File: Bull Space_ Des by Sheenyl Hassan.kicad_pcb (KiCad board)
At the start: 2 copper layers, 10 parts, among them IC1 TEENSY_4.0, IC2 XB24CZ7PIT-004, U1 Regulator_Linear_AP2204RB-3.3, U2 Flight-Computer_Adafruit_GPS_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, U3 ADXL343, U4 BMP280, U6 Memory_Flash_W25Q32JVSS

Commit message: Add files via upload
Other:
- net class Default removed

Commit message: Updates
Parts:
- moved IC1 53.4 mm to (81.3, 114.3)
- moved IC2 50.0 mm to (206.8, 109.7)
- moved U2 36.5 mm to (99.9, 142.2)
- moved U3 32.6 mm to (165.1, 114.3)
- moved U1 30.5 mm to (182.9, 81.3)
- moved U6 21.3 mm to (147.3, 142.2)
- moved U4 20.3 mm to (119.4, 86.4)
- moved C1 12.0 mm to (142.2, 99.1)
- moved C5 10.9 mm to (154.9, 78.7)
- moved R1 9.67 mm to (157.5, 129.5)
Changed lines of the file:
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@@
   (net 68 "Net-(U2-Pad9)")
   (footprint "KiCad:TEENSY40" (layer "F.Cu")
-    (at 134.62 115.57)
+    (at 81.28 114.3)
     (descr "TEENSY 4.0-4")
     (tags "Integrated Circuit")
@@
   )
   (footprint "Package_LGA:LGA-14_3x5mm_P0.8mm_LayoutBorder1x6y" (layer "F.Cu")
-    (at 153.67 83.82 90)
+    (at 165.1 114.3 90)
     (descr "LGA, 14 Pin (http://www.st.com/resource/en/datasheet/lsm303dlhc.pdf), generated with kicad-footprint-generator ipc_noLead_generator.py")
     (tags "LGA NoLead")
@@
   )
   (footprint "Package_SO:SOIC-8_5.23x5.23mm_P1.27mm" (layer "F.Cu")
-    (at 153.67 121.92)
+    (at 147.32 142.24)
     (descr "SOIC, 8 Pin (http://www.winbond.com/resource-files/w25q32jv%20revg%2003272018%20plus.pdf#page=68), generated with kicad-footprint-generator ipc_gullwing_generator.py")
     (tags "SOIC SO")
@@
   )
   (footprint "Capacitor_SMD:C_0603_1608Metric_Pad1.08x0.95mm_HandSolder" (layer "F.Cu")
-    (at 146.05 87.63 180)
+    (at 142.24 99.06 180)
     (descr "Capacitor SMD 0603 (1608 Metric), square (rectangular) end terminal, IPC_7351 nominal with elongated pad for handsoldering. (Body size source: IPC-SM-782 page 76, https://www.pcb-3d.com/wordpress/wp-content/uploads/ipc-sm-782a_amendment_1_and_2.pdf), generated with kicad-footprint-generator")
     (tags "capacitor handsolder")
@@
   )
   (footprint "Capacitor_SMD:C_0603_1608Metric_Pad1.08x0.95mm_HandSolder" (layer "F.Cu")
-    (at 146.05 85.12 180)
+    (at 154.94 78.74 180)
     (descr "Capacitor SMD 0603 (1608 Metric), square (rectangular) end terminal, IPC_7351 nominal with elongated pad for handsoldering. (Body size source: IPC-SM-782 page 76, https://www.pcb-3d.com/wordpress/wp-content/uploads/ipc-sm-782a_amendment_1_and_2.pdf), generated with kicad-footprint-generator")
     (tags "capacitor handsolder")
@@
   )
   (footprint "Package_TO_SOT_SMD:SOT-89-3" (layer "F.Cu")
-    (at 153.67 90.17 -90)
+    (at 182.88 81.28 -90)
     (descr "SOT-89-3, http://ww1.microchip.com/downloads/en/DeviceDoc/3L_SOT-89_MB_C04-029C.pdf")
     (tags "SOT-89-3")
@@
   )
   (footprint "Resistor_SMD:R_0603_1608Metric_Pad0.98x0.95mm_HandSolder" (layer "F.Cu")
-    (at 161.29 120.65 -90)
+    (at 157.48 129.54 -90)
     (descr "Resistor SMD 0603 (1608 Metric), square (rectangular) end terminal, IPC_7351 nominal with elongated pad for handsoldering. (Body size source: IPC-SM-782 page 72, https://www.pcb-3d.com/wordpress/wp-content/uploads/ipc-sm-782a_amendment_1_and_2.pdf), generated with kicad-footprint-generator")
     (tags "resistor handsolder")
@@
   )
   (footprint "KiCad:XB24CAPIT-001" (layer "F.Cu")
-    (at 162.56 86.36 -90)
+    (at 206.77 109.702955 -90)
     (descr "Digi XBee 802.15.4")
     (tags "Integrated Circuit")
@@
   )
   (footprint "KiCad:Flight-Computer_Adafruit_GPS_THT_Footprint" (layer "F.Cu")
-    (at 134.62 130.81 -90)
+    (at 99.917 142.24 -90)
     (attr through_hole)
     (fp_text reference "U2" (at 0.508 2.032 90) (layer "F.SilkS")
@@
   )
   (footprint "Package_LGA:Bosch_LGA-8_2x2.5mm_P0.65mm_ClockwisePinNumbering" (layer "F.Cu")
-    (at 139.7 86.36)
+    (at 119.38 86.36)
     (descr "LGA-8, https://ae-bst.resource.bosch.com/media/_tech/media/datasheets/BST-BMP280-DS001-18.pdf")
     (tags "lga land grid array")

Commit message: Added Ignition
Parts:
- added BZ1: Buzzer, Buzzer_Beeper:Buzzer_12x9.5RM7.6, F.Cu at (103.1, 74.4)
- added C2: 1uf, Capacitor_SMD:C_0805_2012Metric_Pad1.18x1.45mm_HandSolder, F.Cu at (78.7, 127.0)
- added C3: 22uf, Capacitor_SMD:C_0805_2012Metric_Pad1.18x1.45mm_HandSolder, F.Cu at (47.2, 96.8)
- added C4: 47pf, Capacitor_SMD:C_0805_2012Metric_Pad1.18x1.45mm_HandSolder, F.Cu at (84.1, 131.6)
- added D1: LED_ABGR, LED_THT:LED_D5.0mm-4_RGB_Staggered_Pins, F.Cu at (112.6, 43.2)
- added J1: Screw_Terminal_01x02, TerminalBlock:TerminalBlock_bornier-2_P5.08mm, F.Cu at (80.8, 40.6)
- added J2: Screw_Terminal_01x02, TerminalBlock:TerminalBlock_bornier-2_P5.08mm, F.Cu at (80.8, 52.7)
- added R2: 220, Resistor_SMD:R_0603_1608Metric_Pad0.98x0.95mm_HandSolder, F.Cu at (124.0, 50.5)
- added R3: 220, Resistor_SMD:R_0603_1608Metric_Pad0.98x0.95mm_HandSolder, F.Cu at (127.0, 45.7)
- added R4: 220, Resistor_SMD:R_0603_1608Metric_Pad0.98x0.95mm_HandSolder, F.Cu at (122.9, 40.6)
- C1, C5: footprint Capacitor_SMD:C_0603_1608Metric_Pad1.08x0.95mm_HandSolder -> Capacitor_SMD:C_0805_2012Metric_Pad1.18x1.45mm_HandSolder
- IC1: footprint KiCad:TEENSY40 -> Flight Computer:Teensy40
- IC2: footprint KiCad:XB24CAPIT-001 -> Flight Computer:XBEE_PRO_PTH
- U2: footprint KiCad:Flight-Computer_Adafruit_GPS_THT_Footprint -> Flight Computer:Adafruit_ADXL345_THT
- moved IC2 125.9 mm to (81.3, 119.4), turned to 0 degrees
- moved U3 114.3 mm to (50.8, 111.8), turned to 180 degrees
- moved U6 100.1 mm to (55.9, 101.6)
- moved R1 95.6 mm to (66.0, 101.6), turned to 180 degrees
- moved U4 75.4 mm to (55.9, 127.0)
- moved U1 53.8 mm to (130.6, 68.6)
- moved C1 39.3 mm to (125.5, 63.5)
- moved U2 38.3 mm to (96.0, 104.1)
- moved IC1 25.4 mm to (81.3, 88.9), turned to -90 degrees
- moved C5 24.0 mm to (136.4, 63.5)
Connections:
- net XBEE-RX renamed /XBEE-TX
- net XBEE-TX renamed /XBEE-RX
- IC1 pad 10: Net-(IC1-Pad10) -> /FL-CS
- IC1 pad 11: Net-(IC1-Pad11) -> /BMP-CS
- IC1 pad 12: FL-CS -> /ADXL-CS
- IC1 pad 13: MOSI -> /MOSI
- IC1 pad 14: MISO -> /MISO
- IC1 pad 15: Net-(IC1-Pad15) -> unconnected-(IC1-Pad15)
- IC1 pad 16: Net-(IC1-Pad16) -> +3V3
- IC1 pad 18: Net-(IC1-Pad18) -> unconnected-(IC1-Pad18)
- IC1 pad 19: Net-(IC1-Pad19) -> unconnected-(IC1-Pad19)
- IC1 pad 2: Net-(IC1-Pad2) -> unconnected-(IC1-Pad2)
- IC1 pad 20: SCK -> /SCK
- IC1 pad 23: SCL -> unconnected-(IC1-Pad23)
- IC1 pad 24: SDA -> unconnected-(IC1-Pad24)
- IC1 pad 25: Net-(IC1-Pad25) -> unconnected-(IC1-Pad25)
- IC1 pad 26: Net-(IC1-Pad26) -> unconnected-(IC1-Pad26)
- IC1 pad 27: Net-(IC1-Pad27) -> /GPS-RX
- IC1 pad 28: Net-(IC1-Pad28) -> /GPS-TX
- IC1 pad 29: Net-(IC1-Pad29) -> unconnected-(IC1-Pad29)
- IC1 pad 3: Net-(IC1-Pad3) -> unconnected-(IC1-Pad3)
- IC1 pad 30: Net-(IC1-Pad30) -> unconnected-(IC1-Pad30)
- IC1 pad 33: +5V -> unconnected-(IC1-Pad33)
- IC1 pad 4: Net-(IC1-Pad4) -> LED-R
- IC1 pad 5: Net-(IC1-Pad5) -> LED-G
- IC1 pad 6: Net-(IC1-Pad6) -> LED-B
- IC1 pad 7: Net-(IC1-Pad7) -> unconnected-(IC1-Pad7)
- IC1 pad 8: Net-(IC1-Pad8) -> unconnected-(IC1-Pad8)
- IC1 pad 9: Net-(IC1-Pad9) -> unconnected-(IC1-Pad9)
- IC2 pad 11: Net-(IC2-Pad11) -> unconnected-(IC2-Pad11)
- IC2 pad 12: Net-(IC2-Pad12) -> unconnected-(IC2-Pad12)
- IC2 pad 13: Net-(IC2-Pad13) -> unconnected-(IC2-Pad13)
- IC2 pad 14: Net-(IC2-Pad14) -> unconnected-(IC2-Pad14)
- IC2 pad 15: Net-(IC2-Pad15) -> unconnected-(IC2-Pad15)
- IC2 pad 16: Net-(IC2-Pad16) -> unconnected-(IC2-Pad16)
- IC2 pad 17: Net-(IC2-Pad17) -> unconnected-(IC2-Pad17)
- IC2 pad 18: Net-(IC2-Pad18) -> unconnected-(IC2-Pad18)
- IC2 pad 19: Net-(IC2-Pad19) -> unconnected-(IC2-Pad19)
- IC2 pad 20: Net-(IC2-Pad20) -> unconnected-(IC2-Pad20)
- IC2 pad 4: Net-(IC2-Pad4) -> unconnected-(IC2-Pad4)
- IC2 pad 5: Net-(IC2-Pad5) -> unconnected-(IC2-Pad5)
- IC2 pad 6: Net-(IC2-Pad6) -> unconnected-(IC2-Pad6)
- IC2 pad 7: Net-(IC2-Pad7) -> unconnected-(IC2-Pad7)
- IC2 pad 8: Net-(IC2-Pad8) -> unconnected-(IC2-Pad8)
- IC2 pad 9: Net-(IC2-Pad9) -> unconnected-(IC2-Pad9)
- U2 pad 2: Net-(U2-Pad2) -> unconnected-(U2-Pad2)
- U2 pad 3: Net-(U2-Pad3) -> unconnected-(U2-Pad3)
- U2 pad 4: Net-(U2-Pad4) -> unconnected-(U2-Pad4)
- U2 pad 5: SDA -> /GPS-TX
- U2 pad 6: SCL -> /GPS-RX
- U2 pad 8: Net-(U2-Pad8) -> unconnected-(U2-Pad8)
- U2 pad 9: Net-(U2-Pad9) -> unconnected-(U2-Pad9)
- U3 pad 1: Net-(U3-Pad1) -> +3V3
- U3 pad 10: Net-(U3-Pad10) -> unconnected-(U3-Pad10)
- U3 pad 11: Net-(U3-Pad11) -> unconnected-(U3-Pad11)
- U3 pad 12: Net-(U3-Pad12) -> /MISO
- U3 pad 13: SDA -> /MOSI
- U3 pad 14: SCL -> /SCK
- U3 pad 3: Net-(U3-Pad3) -> unconnected-(U3-Pad3)
- U3 pad 7: Net-(U3-Pad7) -> /ADXL-CS
- U3 pad 8: Net-(U3-Pad8) -> unconnected-(U3-Pad8)
- U3 pad 9: Net-(U3-Pad9) -> unconnected-(U3-Pad9)
- U4 pad 2: Net-(U4-Pad2) -> /BMP-CS
- U4 pad 3: SDA -> /MOSI
- U4 pad 4: SCL -> /SCK
- U4 pad 5: Net-(U4-Pad5) -> /MISO
- U4 pad 6: Net-(U4-Pad6) -> +3V3
- U4 pad 7: Net-(U4-Pad7) -> GND
- U4 pad 8: Net-(U4-Pad8) -> +3V3
- U6 pad 1: FL-CS -> /FL-CS
- U6 pad 2: MISO -> /MISO
- U6 pad 3: Net-(U6-Pad3) -> unconnected-(U6-Pad3)
- U6 pad 5: MOSI -> /MOSI
- U6 pad 6: SCK -> /SCK
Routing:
- net +3V3: track 0.00 -> 15.5 mm
- net Net-(R1-Pad2): track 0.00 -> 5.91 mm

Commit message: Board Layout (kinda)
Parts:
- removed J2: Screw_Terminal_01x02, TerminalBlock:TerminalBlock_bornier-2_P5.08mm
- added F1: 3A Polyfuse, Fuse:Fuse_1206_3216Metric_Pad1.42x1.75mm_HandSolder, F.Cu at (87.5, 127.8)
- added F2: 3A Polyfuse, Fuse:Fuse_1206_3216Metric_Pad1.42x1.75mm_HandSolder, F.Cu at (81.8, 128.0)
- added H1: MountingHole, MountingHole:MountingHole_2.7mm_M2.5, F.Cu at (113.8, 138.0)
- added H2: MountingHole, MountingHole:MountingHole_2.7mm_M2.5, F.Cu at (114.0, 67.0)
- added H3: MountingHole, MountingHole:MountingHole_2.7mm_M2.5, F.Cu at (75.0, 138.0)
- added Q1: AOI21357, Package_TO_SOT_THT:TO-251-3_Vertical, F.Cu at (105.6, 121.0)
- added Q2: 2N7002, Package_TO_SOT_SMD:SOT-23, F.Cu at (89.3, 123.8)
- added Q3: 2N7002, Package_TO_SOT_SMD:SOT-23, F.Cu at (98.2, 123.5)
- added Q4: 2N7002, Package_TO_SOT_SMD:SOT-23, F.Cu at (83.5, 123.2)
- added Q5: AOI21357, Package_TO_SOT_THT:TO-251-3_Vertical, F.Cu at (105.6, 113.3)
- added R10: 10k, Resistor_SMD:R_0603_1608Metric_Pad0.98x0.95mm_HandSolder, F.Cu at (86.0, 134.5)
- added R12: 10k, Resistor_SMD:R_0603_1608Metric_Pad0.98x0.95mm_HandSolder, F.Cu at (84.0, 131.8)
- added R5: 100R, Resistor_SMD:R_0603_1608Metric_Pad0.98x0.95mm_HandSolder, F.Cu at (82.0, 136.0)
- added R6: 100R, Resistor_SMD:R_0603_1608Metric_Pad0.98x0.95mm_HandSolder, F.Cu at (80.5, 132.0)
- added R7: 100, Resistor_SMD:R_0603_1608Metric_Pad0.98x0.95mm_HandSolder, F.Cu at (94.2, 127.5)
- added R8: 10k, Resistor_SMD:R_0603_1608Metric_Pad0.98x0.95mm_HandSolder, F.Cu at (86.8, 139.2)
- added R9: 10k, Resistor_SMD:R_0603_1608Metric_Pad0.98x0.95mm_HandSolder, F.Cu at (87.5, 131.5)
- C1: value 1uf -> 10uf
- J1: value Screw_Terminal_01x02 -> Screw_Terminal_01x06; footprint TerminalBlock:TerminalBlock_bornier-2_P5.08mm -> TerminalBlock_4Ucon:TerminalBlock_4Ucon_1x06_P3.50mm_Horizontal
- U1: value Regulator_Linear_AP2204RB-3.3 -> VXO7803-1000; footprint Package_TO_SOT_SMD:SOT-89-3 -> Package_TO_SOT_THT:TO-220-3_Horizontal_TabDown
- U2: footprint Flight Computer:Adafruit_ADXL345_THT -> Flight Computer:Adafruit_GPS_THT
- moved J1 87.8 mm to (111.9, 122.8), turned to 90 degrees
- moved C5 64.2 mm to (101.2, 117.2), turned to 90 degrees
- moved BZ1 60.0 mm to (98.8, 134.2), turned to 180 degrees
- moved U4 58.4 mm to (81.5, 74.5)
- moved U1 58.0 mm to (98.7, 117.0), turned to 90 degrees
- moved C4 57.0 mm to (95.8, 75.8)
- moved C3 56.7 mm to (103.0, 86.2)
- moved C1 55.1 mm to (101.2, 113.0), turned to -90 degrees
- moved C2 51.9 mm to (95.8, 78.0)
- moved IC2 49.7 mm to (103.2, 74.8)
- moved U6 48.5 mm to (103.0, 90.2)
- moved R1 44.9 mm to (109.2, 89.5), turned to -90 degrees
- moved R4 43.0 mm to (94.0, 72.5), turned to -90 degrees
- moved R3 41.2 mm to (95.8, 72.5), turned to -90 degrees
- moved U3 39.6 mm to (81.5, 86.8)
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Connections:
- BZ1 pad 2: GND -> Net-(BZ1-Pad2)
- C1 pad 1: +3V3 -> +BATT
- C5 pad 1: 12V -> +3V3
- IC1 pad 7: unconnected-(IC1-Pad7) -> BUZZER
- IC1 pad 8: unconnected-(IC1-Pad8) -> /ACT1
- IC1 pad 9: unconnected-(IC1-Pad9) -> /ACT2
- J1 pad 1: BATT+ -> +BATT
- U1 pad 1: 12V -> +3V3
- U1 pad 3: +3V3 -> +BATT
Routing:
- net +3V3: track 15.5 -> 3.88 mm, vias 0 -> 1
- net /DROGUE_POW: track 0.00 -> 6.57 mm
- net /MAIN_POW: track 0.00 -> 6.30 mm
- net Net-(R1-Pad2): track 5.91 -> 0.00 mm
- added copper zone on B.Cu, net +3V3
- added copper zone on F.Cu, net GND
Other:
- board outline added: 45 x 77 mm

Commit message: Something
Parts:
- moved F2 30.3 mm to (111.8, 132.1), turned to 180 degrees
- moved F1 24.3 mm to (111.8, 127.0), turned to 180 degrees
- moved R7 15.8 mm to (78.7, 124.5), turned to 90 degrees
- moved R8 15.0 mm to (101.6, 137.2), turned to -90 degrees
- moved Q2 14.8 mm to (101.6, 132.1)
- moved R9 13.5 mm to (99.1, 124.5), turned to -90 degrees
- moved R12 12.4 mm to (94.0, 124.5), turned to -90 degrees
- moved R5 11.7 mm to (83.8, 124.5), turned to -90 degrees
- moved Q4 11.5 mm to (76.2, 132.1), turned to -90 degrees
- moved R6 11.3 mm to (88.9, 124.5), turned to -90 degrees
- moved BZ1 9.86 mm to (88.9, 134.6)
- moved Q3 9.54 mm to (94.0, 132.1)
- moved R10 8.41 mm to (94.0, 137.2), turned to -90 degrees
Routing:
- net GND: track 0.00 -> 45.4 mm, vias 0 -> 1
- net Net-(Q3-Pad3): track 0.00 -> 29.8 mm, vias 0 -> 2
- net Net-(Q2-Pad1): track 0.00 -> 21.9 mm
- net Net-(Q1-Pad1): track 0.00 -> 21.5 mm, vias 0 -> 2
- net Net-(F1-Pad2): track 0.00 -> 20.8 mm, vias 0 -> 1
- net Net-(F2-Pad2): track 0.00 -> 20.8 mm, vias 0 -> 1
- net Net-(Q3-Pad1): track 0.00 -> 19.0 mm
- net +BATT: track 0.00 -> 9.89 mm
- net Net-(Q4-Pad1): track 0.00 -> 6.43 mm
- net Net-(BZ1-Pad2): track 0.00 -> 5.76 mm
- net BUZZER: track 0.00 -> 1.63 mm, vias 0 -> 1
- net /ACT2: track 0.00 -> 1.63 mm, vias 0 -> 1
- net /ACT1: track 0.00 -> 1.63 mm, vias 0 -> 1

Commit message: Pyro Channels
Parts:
- moved F2 24.3 mm to (102.8, 109.5), turned to 90 degrees
- moved F1 13.5 mm to (102.8, 117.0), turned to -90 degrees
- moved C1 11.3 mm to (98.8, 102.0)
- moved U1 6.73 mm to (96.2, 110.8)
- moved C5 3.85 mm to (98.8, 114.3)
- moved Q1 1.44 mm to (106.2, 119.8)
- moved Q5 1.22 mm to (106.2, 112.2)
- moved U2 0.25 mm to (72.2, 115.2)
- moved J1 0.15 mm to (111.8, 122.8)
- moved R9 0.06 mm to (99.0, 124.5)
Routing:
- net GND: track 45.4 -> 0.00 mm, vias 1 -> 0
- net +BATT: track 9.89 -> 41.0 mm
- net Net-(Q3-Pad3): track 29.8 -> 2.58 mm, vias 2 -> 0
- net Net-(Q1-Pad1): track 21.5 -> 3.60 mm, vias 2 -> 1
- net Net-(F1-Pad2): track 20.8 -> 3.93 mm, vias 1 -> 0
- net Net-(F2-Pad2): track 20.8 -> 4.31 mm, vias 1 -> 0
- net +3V3: track 4.38 -> 7.12 mm, vias 1 -> 2
- net BUZZER: track 1.63 -> 0.00 mm, vias 1 -> 0
- net /ACT2: track 1.63 -> 0.00 mm, vias 1 -> 0
- net /ACT1: track 1.63 -> 0.00 mm, vias 1 -> 0
- net /DROGUE_POW: track 6.57 -> 5.74 mm

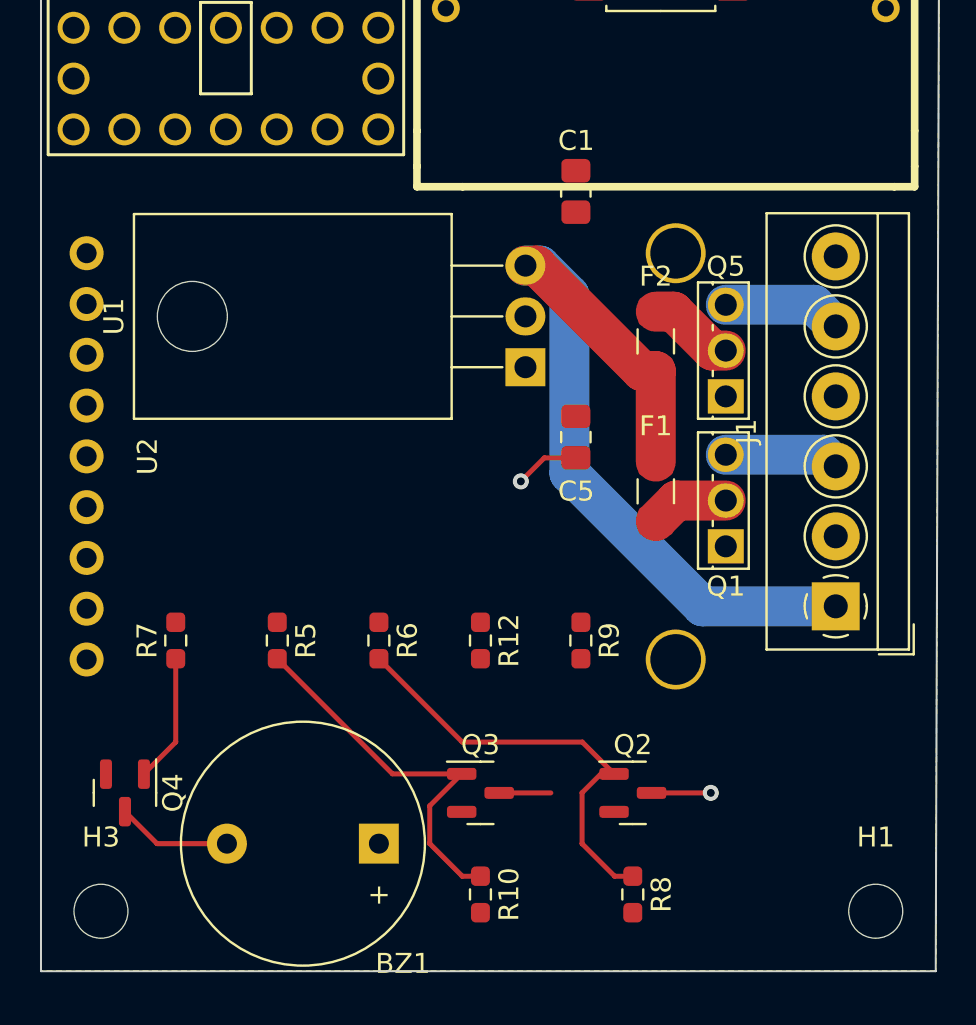
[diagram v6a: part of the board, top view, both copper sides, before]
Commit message: Pyro channels and power supply mods
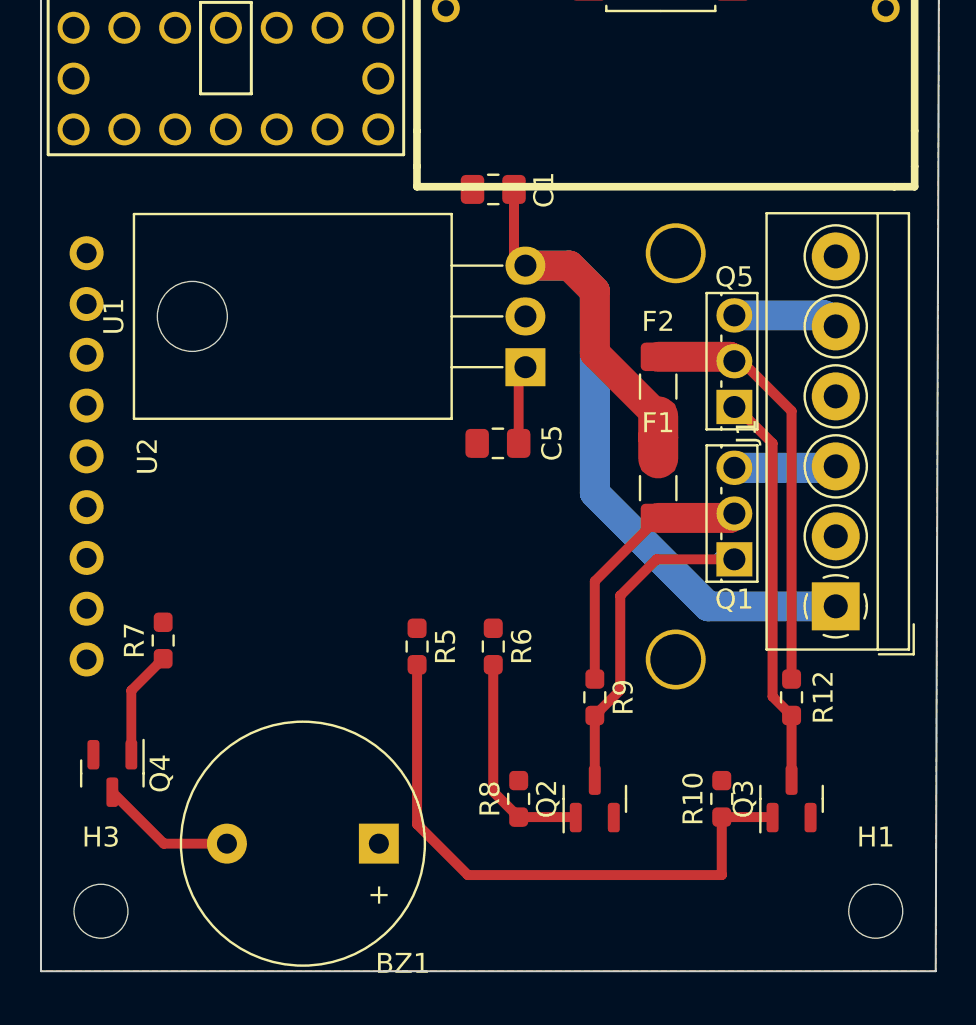
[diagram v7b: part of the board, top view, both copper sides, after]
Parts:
- moved R12 15.8 mm to (109.5, 127.3)
- moved Q3 15.6 mm to (109.5, 132.4), turned to 90 degrees
- moved R10 13.0 mm to (106.0, 132.4), turned to 90 degrees
- moved R8 7.45 mm to (95.9, 132.4), turned to 90 degrees
- moved R5 7.00 mm to (90.8, 124.8)
- moved R6 5.73 mm to (94.6, 124.8)
- moved C1 4.13 mm to (94.6, 101.9), turned to 180 degrees
- moved C5 3.91 mm to (94.9, 114.6), turned to 180 degrees
- moved R9 2.92 mm to (99.7, 127.3)
- moved F2 2.26 mm to (102.9, 111.8)
- moved Q2 1.92 mm to (99.7, 132.4), turned to 90 degrees
- moved Q4 1.16 mm to (75.6, 131.1)
- moved Q1 0.78 mm to (106.7, 120.4)
- moved Q5 0.68 mm to (106.7, 112.8)
- moved R7 0.63 mm to (78.1, 124.5)
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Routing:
- net Net-(Q3-Pad3): track 2.58 -> 19.9 mm
- net Net-(F2-Pad2): track 4.31 -> 21.2 mm
- net Net-(Q1-Pad1): track 3.60 -> 16.8 mm, vias 1 -> 0
- net Net-(Q2-Pad1): track 21.9 -> 11.0 mm
- net Net-(Q3-Pad1): track 19.0 -> 29.7 mm
- net Net-(F1-Pad2): track 3.93 -> 13.3 mm
- net +BATT: track 41.0 -> 46.2 mm
- net Net-(BZ1-Pad2): track 5.76 -> 6.80 mm
- net Net-(Q4-Pad1): track 6.43 -> 5.46 mm
- net +3V3: track 7.12 -> 7.83 mm, vias 2 -> 1
- net /MAIN_POW: track 5.95 -> 5.30 mm
- net /DROGUE_POW: track 5.74 -> 5.10 mm
